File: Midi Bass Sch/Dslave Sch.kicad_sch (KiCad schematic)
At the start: 12 parts, among them J11 D SLAVE ISCP, SW5 D-slave Reset, U9 PIC16F1789

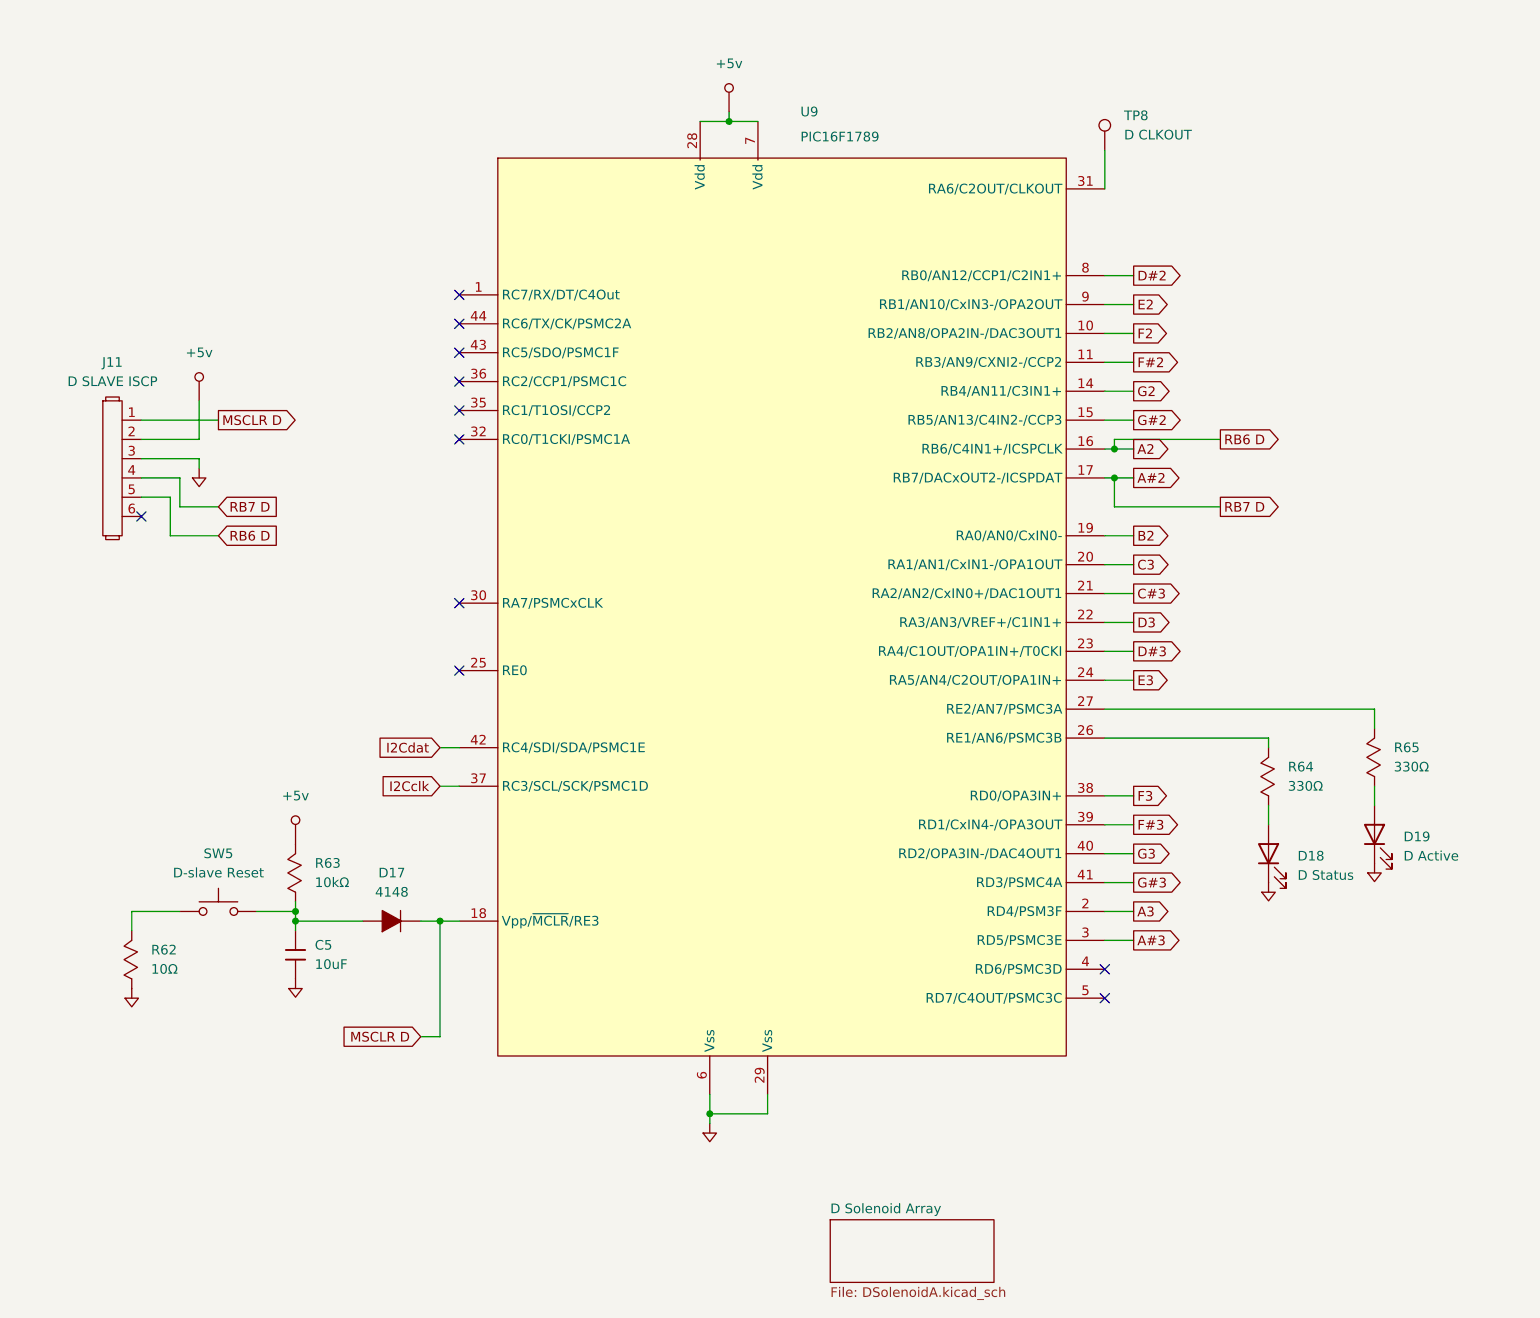
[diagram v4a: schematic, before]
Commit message: began working on pcb layout deleted extra schematics for solenoid break out board
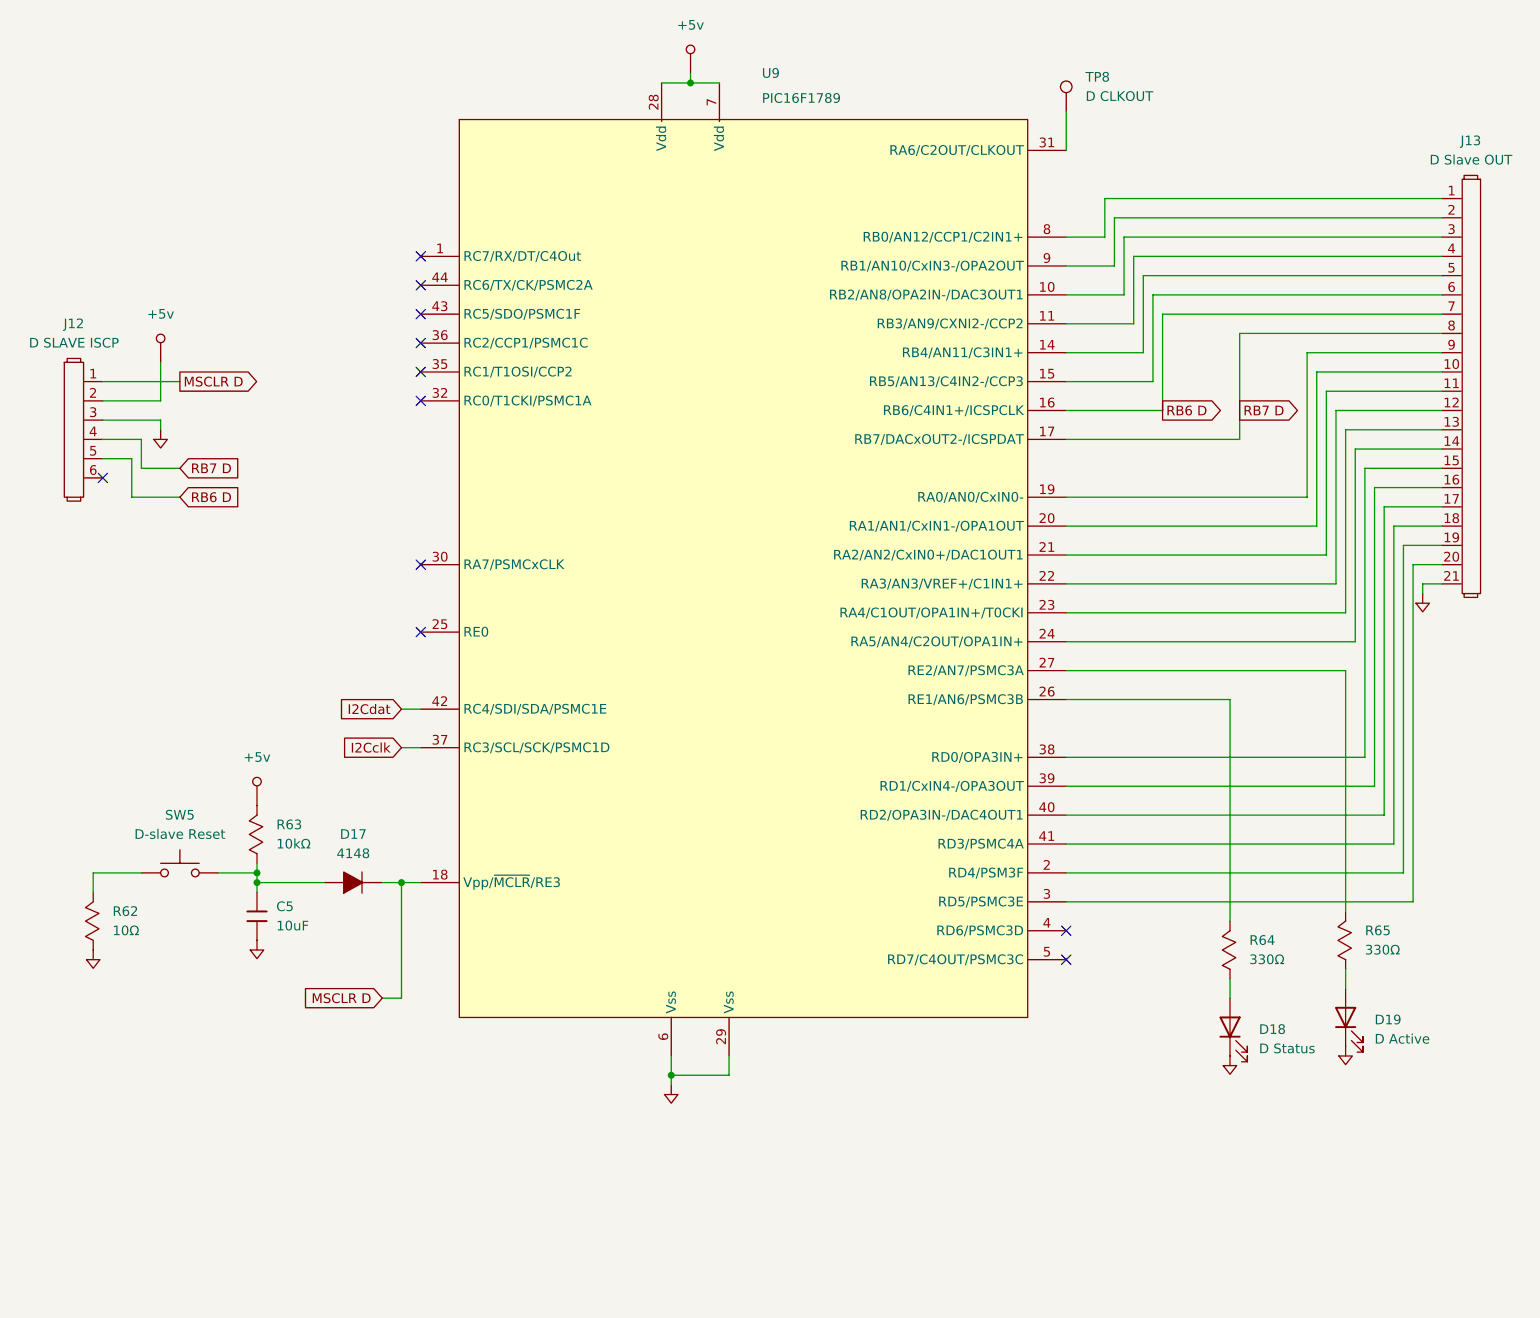
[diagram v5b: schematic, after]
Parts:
- added J13: D Slave OUT, Connector_PinHeader_2.54mm:PinHeader_1x21_P2.54mm_Vertical, symbol Owen's Symbols:Header_1x21
- SW5: footprint (none) -> Button_Switch_THT:SW_PUSH_6mm_H5mm
- TP8: footprint (none) -> Connector_PinHeader_2.54mm:PinHeader_1x01_P2.54mm_Vertical
- U9: footprint (none) -> OF footprints:TQFN-44_7x7_Pitch0.4mm
- renumbered J11 to J12
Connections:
- net GND: now also J13.21
- net A#2 renamed RB7 D
- net RB7 D: now also J13.8
- net A#3: no longer names the net of U9.3 (RD5/PSMC3E)
- net A#3: now also J13.20
- net A2 renamed RB6 D
- net RB6 D: now also J13.7
- net A3: no longer names the net of U9.2 (RD4/PSM3F)
- net A3: now also J13.19
- net B2: no longer names the net of U9.32 (RC0/T1CKI/PSMC1A)
- net B2: now also J13.9
- net C#3: no longer names the net of U9.36 (RC2/CCP1/PSMC1C)
- net C#3: now also J13.11
- net C3: no longer names the net of U9.35 (RC1/T1OSI/CCP2)
- net C3: now also J13.10
- net D#2: no longer names the net of U9.8 (RB0/AN12/CCP1/C2IN1+)
- net D#2: now also J13.1
- net D#3: no longer names the net of U9.42 (RC4/SDI/SDA/PSMC1E)
- net D#3: now also J13.13
- net D3: no longer names the net of U9.37 (RC3/SCL/SCK/PSMC1D)
- net D3: now also J13.12
- net E2: no longer names the net of U9.9 (RB1/AN10/CxIN3-/OPA2OUT)
- net E2: now also J13.2
- net E3: no longer names the net of U9.43 (RC5/SDO/PSMC1F)
- net E3: now also J13.14
- net F#2: no longer names the net of U9.11 (RB3/AN9/CXNI2-/CCP2)
- net F#2: now also J13.4
- net F#3: no longer names the net of U9.39 (RD1/CxIN4-/OPA3OUT)
- net F#3: now also J13.16
- net F2: no longer names the net of U9.10 (RB2/AN8/OPA2IN-/DAC3OUT1)
- net F2: now also J13.3
- net F3: no longer names the net of U9.38 (RD0/OPA3IN+)
- net F3: now also J13.15
- net G#2: no longer names the net of U9.15 (RB5/AN13/C4IN2-/CCP3)
- net G#2: now also J13.6
- net G#3: no longer names the net of U9.41 (RD3/PSMC4A)
- net G#3: now also J13.18
- net G2: no longer names the net of U9.14 (RB4/AN11/C3IN1+)
- net G2: now also J13.5
- net G3: no longer names the net of U9.40 (RD2/OPA3IN-/DAC4OUT1)
- net G3: now also J13.17
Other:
- removed sheet D Solenoid Array
- moved on the sheet: C5, D17, D18, D19, J12, R62, R63, R64, R65, SW5, TP8, U9
